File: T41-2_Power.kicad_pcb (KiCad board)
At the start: 2 copper layers, 70 x 64 mm, 34 parts, among them J1 Conn_02x08_Odd_Even, J2 Screw_Terminal_01x02, J3 Screw_Terminal_01x02, J4 Screw_Terminal_01x02, U1 R-78CK3.3-0.5, U2 R-78CK5.0-0.5

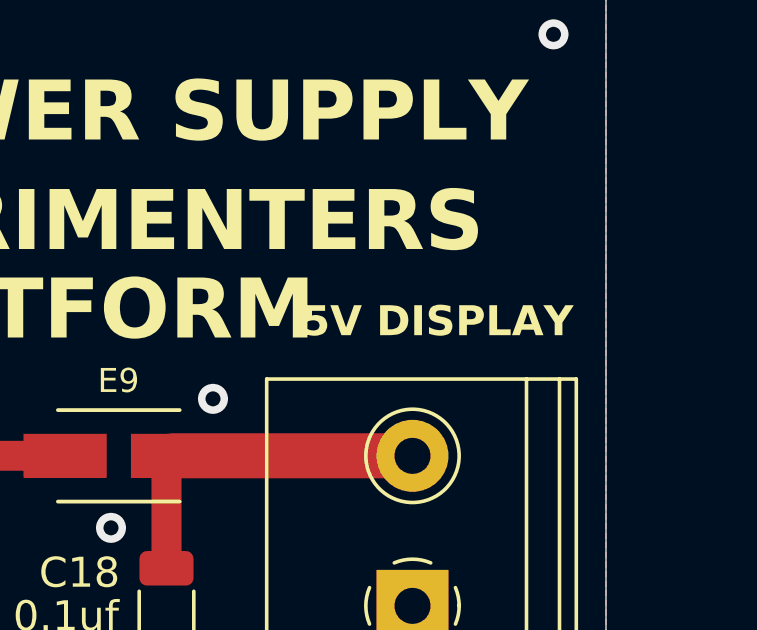
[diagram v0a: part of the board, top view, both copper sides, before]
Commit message: Added + indicator in silkscreen for 5V output.
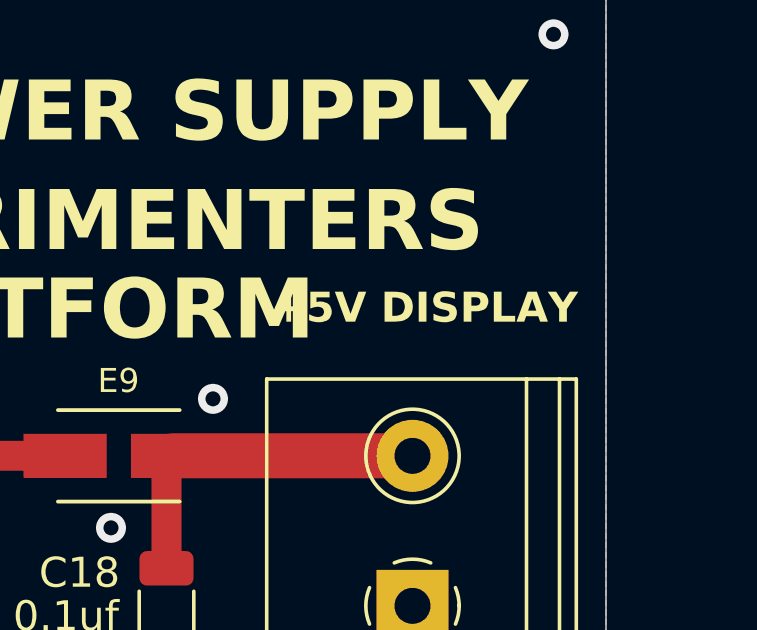
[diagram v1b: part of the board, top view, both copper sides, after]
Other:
- board text added: "+5V DISPLAY"
- board text removed: "5V DISPLAY"
